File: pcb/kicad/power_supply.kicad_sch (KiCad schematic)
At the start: 14 parts, among them U1 HT7533-1, U2 TLV62569DBV

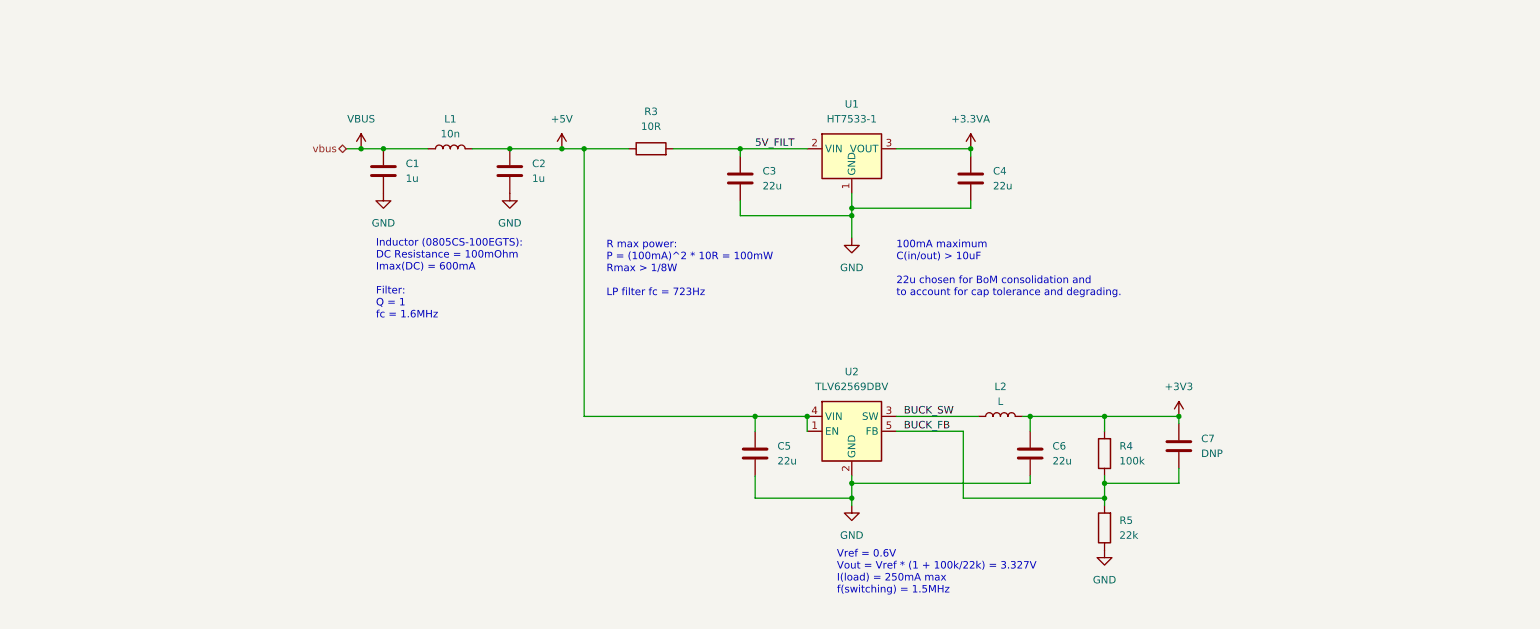
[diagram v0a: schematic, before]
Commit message: Add bias generator.
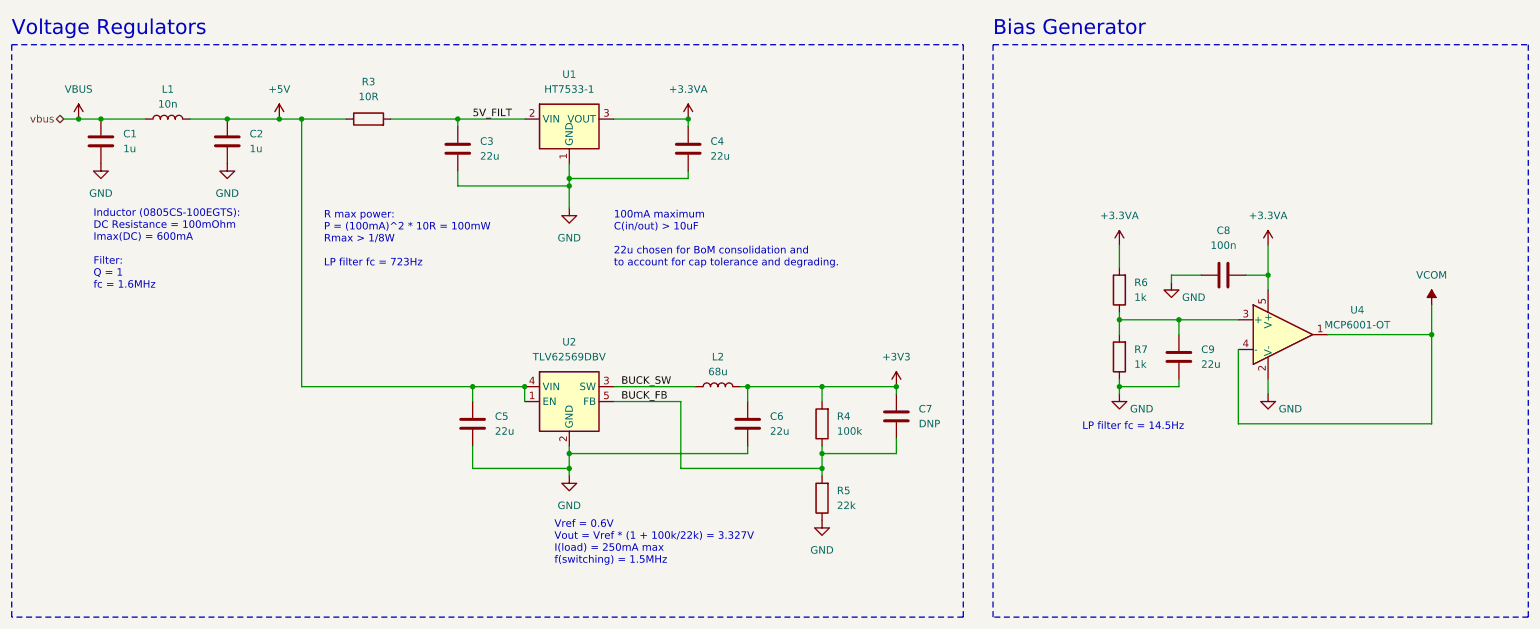
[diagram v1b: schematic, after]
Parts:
- added C8: 100n, Capacitor_SMD:C_0805_2012Metric, symbol Device:C
- added C9: 22u, Capacitor_SMD:C_0805_2012Metric, symbol Device:C
- added R6, R7: 1k, Resistor_SMD:R_0805_2012Metric, symbol Device:R
- added U4: MCP6001-OT, Package_TO_SOT_SMD:SOT-23-5, symbol Amplifier_Operational:MCP6001-OT
- L2: value L -> 68u
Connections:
- net +3.3VA: now also C8.2, R6.2, U4.5 (V+)
- net GND: now also C8.1, C9.2, R7.1, U4.2 (V-)
- new net: C9.1, R6.1, R7.2, U4.3 (+)
- new net VCOM: U4.1, U4.4 (-)
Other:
- note added: "Bias Generator"
- note added: "LP filter fc = 14.5Hz"
- note added: "Voltage Regulators"
- moved on the sheet: C1, C2, C3, C4, C5, C6, C7, L1, L2, R3, R4, R5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

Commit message: Added converters, controls and updated annotations.
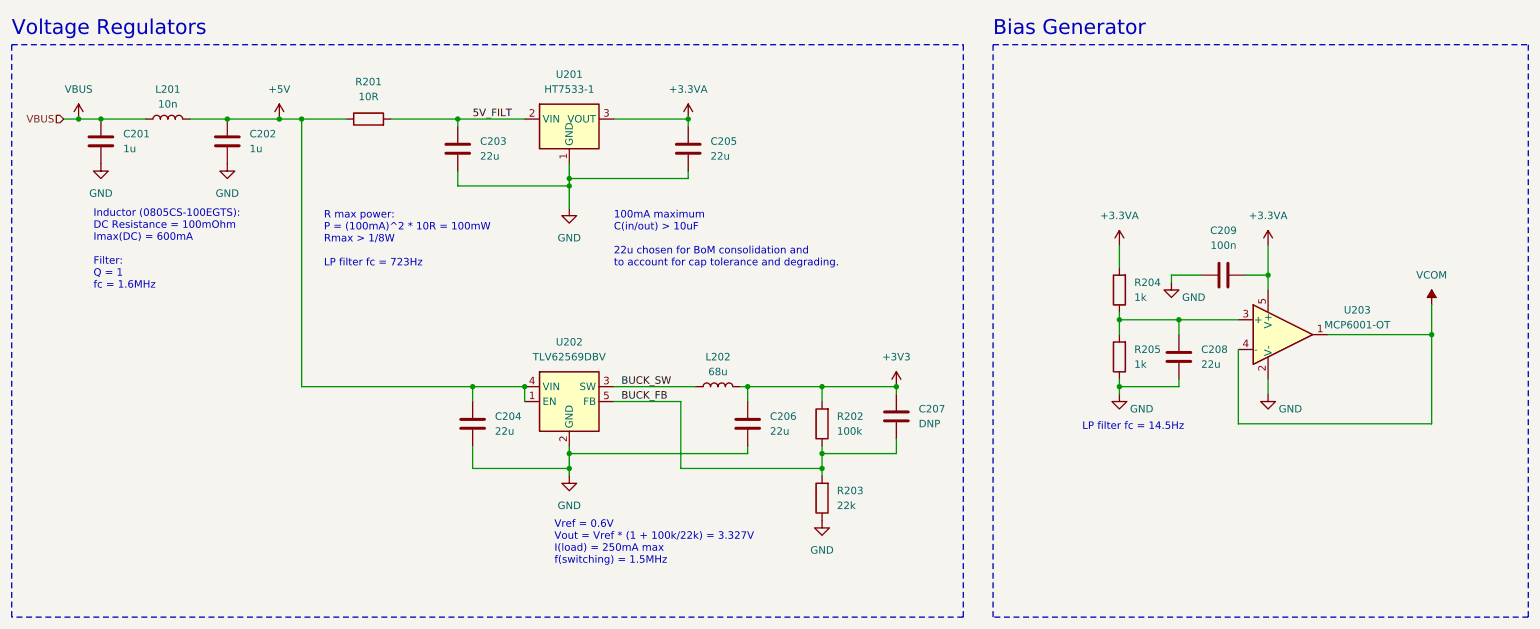
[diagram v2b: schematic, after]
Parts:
- renumbered C1 to C201, C2 to C202, C3 to C203, C5 to C204, C4 to C205, C6 to C206, C7 to C207, C9 to C208, C8 to C209, L1 to L201, L2 to L202, R3 to R201, R4 to R202, R5 to R203, R6 to R204, R7 to R205, U1 to U201, U2 to U202, U4 to U203

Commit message: Added PCB layout and fabrication output.
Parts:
- L202: footprint (none) -> pedal-components:ASPI-4030S-680M-T; Part Number (none) -> ASPI-4030S-680M-T
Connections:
- net VCOM_INPUT: now reaches C208.1, R204.1, R205.2, U203.3 (+)
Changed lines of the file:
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@@
   )
   (text "Vref = 0.6V\nVout = Vref * (1 + 100k/22k) = 3.327V\nI(load) = 250mA max\nf(switching) = 1.5MHz"
-    (at 111.76 138.43 0)
+    (at 105.41 138.43 0)
     (effects (font (size 1.27 1.27)) (justify left bottom))
   )
@@
   )
   (label "BUCK_FB" (at 123.19 110.49 0) (fields_autoplaced)
+    (effects (font (size 1.27 1.27)) (justify left bottom))
+  )
+  (label "VCOM_INPUT" (at 214.63 96.52 0) (fields_autoplaced)
     (effects (font (size 1.27 1.27)) (justify left bottom))
   )
@@
       (effects (font (size 1.27 1.27)))
     )
-    (property "Footprint" "" (at 139.7 107.95 0)
+    (property "Footprint" "pedal-components:ASPI-4030S-680M-T" (at 139.7 107.95 0)
       (effects (font (size 1.27 1.27)) hide)
     )
@@
       (effects (font (size 1.27 1.27)) hide)
     )
+    (property "Part Number" "ASPI-4030S-680M-T" (at 139.7 107.95 90)
+      (effects (font (size 1.27 1.27)) hide)
+    )

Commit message: Add part numbers to components for ordering.
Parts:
- C201, C202: Part Number (none) -> CC0805KKX7R7BB105
- C203, C204, C205, C206, C208: Part Number (none) -> C0805C226M8PAC7210
- C209: Part Number (none) -> CC0805JRX7R9BB104
- L201: Part Number (none) -> 0805CS-100EGTS
- L202: Supplier Link (none) -> https://www.digikey.de/en/products/detail/abracon-llc/ASPI-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
- R201: Part Number (none) -> RNCP0805FTD10R0
- R202: Part Number (none) -> RT0805FRE07100KL
- R203: Part Number (none) -> RT0805FRE1322KL
- R204, R205: Part Number (none) -> RT0805FRE071KL
- U202: Part Number (none) -> TLV62569DBVR; Supplier Link (none) -> https://www.digikey.de/en/products/detail/texas-instruments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
- U203: Part Number (none) -> MCP6001UT-I/OT; Supplier Link (none) -> https://www.digikey.de/en/products/detail/microchip-technol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
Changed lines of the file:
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@@
+      (effects (font (size 1.27 1.27)) hide)
+    )
+    (property "Supplier Link" "" (at 208.28 91.44 0)
+      (effects (font (size 1.27 1.27)) hide)
+    )
+    (property "Part Number" "RT0805FRE071KL" (at 208.28 91.44 0)
       (effects (font (size 1.27 1.27)) hide)
     )
@@
     )
     (property "Datasheet" "~" (at 80.01 62.23 0)
+      (effects (font (size 1.27 1.27)) hide)
+    )
+    (property "Supplier Link" "" (at 80.01 62.23 0)
+      (effects (font (size 1.27 1.27)) hide)
+    )
+    (property "Part Number" "RNCP0805FTD10R0" (at 80.01 62.23 0)
       (effects (font (size 1.27 1.27)) hide)
     )
@@
       (effects (font (size 1.27 1.27)) hide)
     )
+    (property "Part Number" "TLV62569DBVR" (at 114.3 110.49 0)
+      (effects (font (size 1.27 1.27)) hide)
+    )
+    (property "Supplier Link" "https://www.digikey.de/en/products/detail/texas-instruments/TLV62569DBVR/6580119" (at 114.3 110.49 0)
+      (effects (font (size 1.27 1.27)) hide)
+    )
     (pin "1")
     (pin "2")
@@
       (effects (font (size 1.27 1.27)) hide)
     )
+    (property "Supplier Link" "" (at 34.29 66.04 0)
+      (effects (font (size 1.27 1.27)) hide)
+    )
+    (property "Part Number" "CC0805KKX7R7BB105" (at 34.29 66.04 0)
+      (effects (font (size 1.27 1.27)) hide)
+    )
     (pin "1")
     (pin "2")
@@
     )
     (property "Datasheet" "~" (at 144.78 114.3 0)
+      (effects (font (size 1.27 1.27)) hide)
+    )
+    (property "Supplier Link" "" (at 144.78 114.3 0)
+      (effects (font (size 1.27 1.27)) hide)
+    )
+    (property "Part Number" "C0805C226M8PAC7210" (at 144.78 114.3 0)
       (effects (font (size 1.27 1.27)) hide)
     )
@@
       (effects (font (size 1.27 1.27)) hide)
     )
+    (property "Supplier Link" "" (at 218.44 102.87 0)
+      (effects (font (size 1.27 1.27)) hide)
+    )
+    (property "Part Number" "C0805C226M8PAC7210" (at 218.44 102.87 0)
+      (effects (font (size 1.27 1.27)) hide)
+    )
     (pin "1")
     (pin "2")
@@
       (effects (font (size 1.27 1.27)) hide)
     )
+    (property "Supplier Link" "" (at 157.48 114.3 0)
+      (effects (font (size 1.27 1.27)) hide)
+    )
+    (property "Part Number" "RT0805FRE07100KL" (at 157.48 114.3 0)
+      (effects (font (size 1.27 1.27)) hide)
+    )
     (pin "1")
     (pin "2")
@@
       (effects (font (size 1.27 1.27)) hide)
     )
+    (property "Supplier Link" "" (at 226.06 88.9 0)
+      (effects (font (size 1.27 1.27)) hide)
+    )
+    (property "Part Number" "CC0805JRX7R9BB104" (at 226.06 88.9 0)
+      (effects (font (size 1.27 1.27)) hide)
+    )
     (pin "1")
     (pin "2")
@@
       (effects (font (size 1.27 1.27)) hide)
     )
+    (property "Supplier Link" "" (at 45.72 62.23 0)
+      (effects (font (size 1.27 1.27)) hide)
+    )
+    (property "Part Number" "0805CS-100EGTS" (at 45.72 62.23 0)
+      (effects (font (size 1.27 1.27)) hide)
+    )
     (pin "1")
     (pin "2")
@@
       (effects (font (size 1.27 1.27)) hide)
     )
+    (property "Supplier Link" "" (at 134.62 67.31 0)
+      (effects (font (size 1.27 1.27)) hide)
+    )
+    (property "Part Number" "C0805C226M8PAC7210" (at 134.62 67.31 0)
+      (effects (font (size 1.27 1.27)) hide)
+    )
     (pin "1")
     (pin "2")
@@
       (effects (font (size 1.27 1.27)) hide)
     )
+    (property "Supplier Link" "" (at 170.18 113.03 0)
+      (effects (font (size 1.27 1.27)) hide)
+    )
     (pin "1")
     (pin "2")
@@
       (effects (font (size 1.27 1.27)) hide)
     )
+    (property "Supplier Link" "" (at 97.79 114.3 0)
+      (effects (font (size 1.27 1.27)) hide)
+    )
+    (property "Part Number" "C0805C226M8PAC7210" (at 97.79 114.3 0)
+      (effects (font (size 1.27 1.27)) hide)
+    )
     (pin "1")
     (pin "2")
@@
     )
     (property "Datasheet" "~" (at 55.88 66.04 0)
+      (effects (font (size 1.27 1.27)) hide)
+    )
+    (property "Supplier Link" "" (at 55.88 66.04 0)
+      (effects (font (size 1.27 1.27)) hide)
+    )
+    (property "Part Number" "CC0805KKX7R7BB105" (at 55.88 66.04 0)
       (effects (font (size 1.27 1.27)) hide)
     )
@@
       (effects (font (size 1.27 1.27)) hide)
     )
+    (property "Supplier Link" "" (at 114.3 64.77 0)
+      (effects (font (size 1.27 1.27)) hide)
+    )
     (pin "1")
     (pin "2")
@@
       (effects (font (size 1.27 1.27)) hide)
     )
+    (property "Supplier Link" "https://www.digikey.de/en/products/detail/abracon-llc/ASPI-4030S-680M-T/5055591?s=N4IgTCBcDaIIIGUAKBJAtAFgAwGYsLQDYAOLAWTQBUQBdAXyA" (at 139.7 107.95 0)
+      (effects (font (size 1.27 1.27)) hide)
+    )
     (pin "1")
     (pin "2")
@@
     )
     (property "Datasheet" "~" (at 95.25 67.31 0)
+      (effects (font (size 1.27 1.27)) hide)
+    )
+    (property "Supplier Link" "" (at 95.25 67.31 0)
+      (effects (font (size 1.27 1.27)) hide)
+    )
+    (property "Part Number" "C0805C226M8PAC7210" (at 95.25 67.31 0)
       (effects (font (size 1.27 1.27)) hide)
     )
@@
       (effects (font (size 1.27 1.27)) hide)
     )
+    (property "Part Number" "MCP6001UT-I/OT" (at 236.22 99.06 0)
+      (effects (font (size 1.27 1.27)) hide)
+    )
+    (property "Supplier Link" "https://www.digikey.de/en/products/detail/microchip-technology/MCP6001UT-I-OT/562450" (at 236.22 99.06 0)
+      (effects (font (size 1.27 1.27)) hide)
+    )
     (pin "2")
     (pin "5")
@@
       (effects (font (size 1.27 1.27)) hide)
     )
+    (property "Supplier Link" "" (at 208.28 102.87 0)
+      (effects (font (size 1.27 1.27)) hide)
+    )
+    (property "Part Number" "RT0805FRE071KL" (at 208.28 102.87 0)
+      (effects (font (size 1.27 1.27)) hide)
+    )
     (pin "1")
     (pin "2")
@@
       (effects (font (size 1.27 1.27)) hide)
     )
+    (property "Supplier Link" "" (at 157.48 127 0)
+      (effects (font (size 1.27 1.27)) hide)
+    )
+    (property "Part Number" "RT0805FRE1322KL" (at 157.48 127 0)
+      (effects (font (size 1.27 1.27)) hide)
+    )
